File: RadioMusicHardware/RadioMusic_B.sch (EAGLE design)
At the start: 32 parts, among them IC4 TL074, U1 TEENSY_3.1_TW

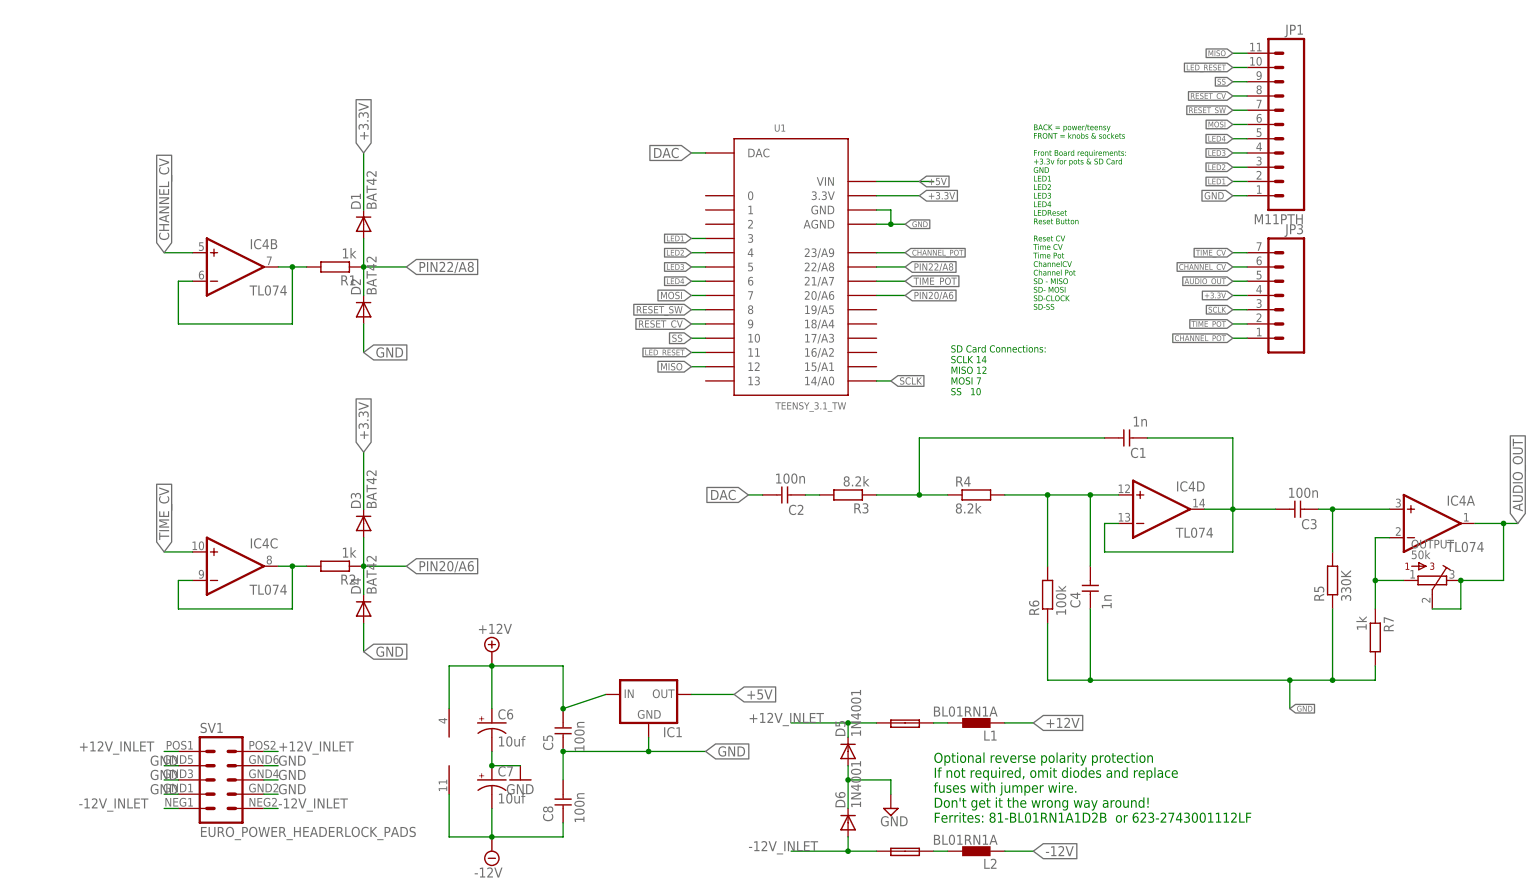
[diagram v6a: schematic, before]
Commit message: Routed Version 2 -  needs to be checked
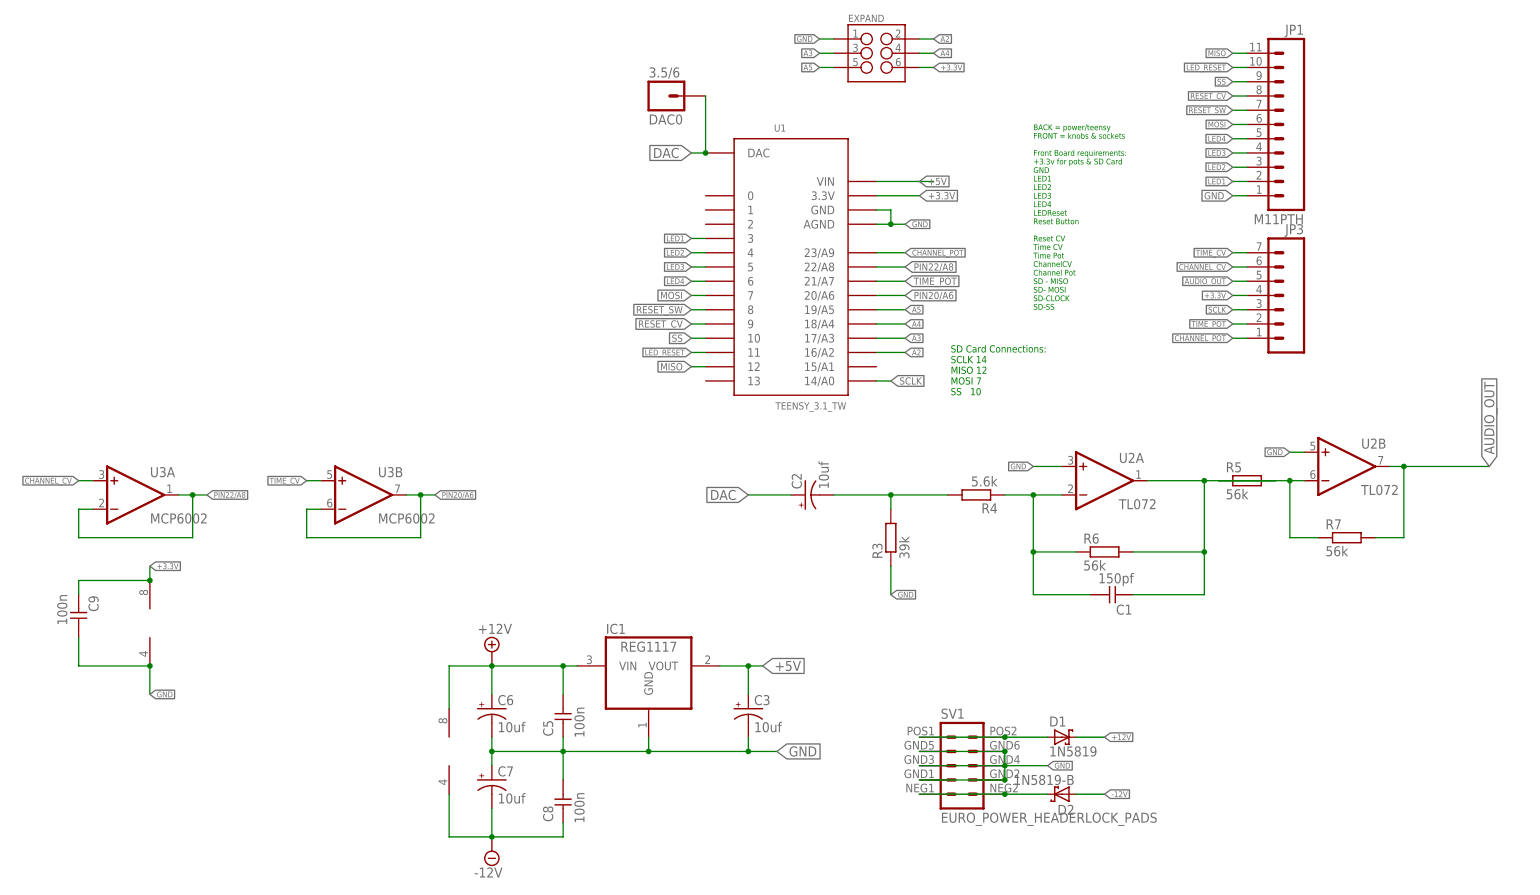
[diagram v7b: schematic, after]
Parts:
- removed C4: 1n, TomW:C-EU050-024X044
- removed D3, D4: BAT42, diode:BAT81
- removed D5, D6: 1N4001, diode:1N4004
- removed F1, F2: FUSE, TomW:PTC_FUSEPOLY_FUSE
- removed IC4: TL074, linear:TL074P
- removed L1, L2: BL01RN1A, inductors:BL01RN1A
- removed OUTPUT: 50k, bourns:3362P
- removed R1, R2: 1k, TomW:R-EU_STANDARD_RESISTOR
- added 3.5/6: DAC0, SparkFun-Connectors:M01PTH
- added C9: 100n, TomW:C-EU050-024X044
- added EXPAND: (no value), SparkFun-Connectors:M03X22X3_SILK_SM
- added U2: TL072, MusicThingModular:TL072
- added U3: MCP6002, MusicThingModular:MCP6002DIL_SMALL
- C1: value 1n -> 150pf
- C2, C3: value 100n -> 10uf; device TomW:C-EU050-025X075 -> SparkFun-Passives:CAP_POLPTH2
- D1: value BAT42 -> 1N5819; device diode:BAT81 -> diode:1N5819-B
- D2: value BAT42 -> 1N5819-B; device diode:BAT81 -> diode:1N5819-B
- IC1: value (none) -> REG1117; device v-reg:78LXX -> burr-brown:REG1117
- R3: value 8.2k -> 39k
- R4: value 8.2k -> 5.6k
- R5: value 330K -> 56k
- R6: value 100k -> 56k
- R7: value 1k -> 56k
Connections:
- removed net +12V_INLET: D5.C, F1.P$1, SV1.10, SV1.9
- removed net -12V_INLET: D6.A, F2.P$1, SV1.1, SV1.2
- removed net N$10: C2.2, R3.2
- removed net N$22: F1.P$2, L1.2
- removed net N$23: F2.P$2, L2.2
- removed net N$6: C3.2, IC4A.+IN, R5.2
- removed net N$7: IC4A.-IN, OUTPUT.1, R7.1
- new net A2: EXPAND.2, U1.16/A2
- new net A3: EXPAND.3, U1.17/A3
- new net A4: EXPAND.4, U1.18/A4
- new net A5: EXPAND.5, U1.19/A5
- new net N$9: D2.C, SV1.1, SV1.2
- net +12V: now also D1.C, IC1.VIN, U2P.V+; no longer IC1.IN, IC4P.V+, L1.1
- net +3.3V: now also C9.2, EXPAND.6, U3P.V+; no longer D1.C, D3.C
- net +5V: now also C3.+, IC1.VOUT; no longer IC1.OUT
- net -12V: now also D2.A, U2P.V-; no longer IC4P.V-, L2.1
- net AUDIO_OUT: now also R7.2, U2B.OUT; no longer IC4A.OUT, OUTPUT.2, OUTPUT.3
- net CHANNEL_CV: now also U3A.+IN; no longer IC4B.+IN
- net DAC: now also 3.5/6.1, C2.+; no longer C2.1
- net GND: now also C3.-, C9.1, EXPAND.1, R3.1, U2A.+IN, U2B.+IN, U3P.V-; no longer C4.2, D2.A, D4.A, D5.A, D6.C, R5.1, R6.1, R7.2
- net N$1: now also C2.-, R3.2, R4.2; no longer IC4C.-IN, IC4C.OUT, R2.2
- net N$2: now also C1.1, R4.1, R6.1, U2A.-IN; no longer C4.1, IC4D.+IN, R4.2, R6.2
- net N$3: now also R5.1, R7.1, U2B.-IN; no longer IC4B.-IN, IC4B.OUT, R1.2
- net N$4: now also C1.2, R5.2, R6.2, U2A.OUT; no longer C1.1, R3.1, R4.1
- net N$5: now also D1.A, SV1.10, SV1.9; no longer C1.2, C3.1, IC4D.-IN, IC4D.OUT
- net PIN20/A6: now also U3B.-IN, U3B.OUT; no longer D3.A, D4.C, R2.1
- net PIN22/A8: now also U3A.-IN, U3A.OUT; no longer D1.A, D2.C, R1.1
- net TIME_CV: now also U3B.+IN; no longer IC4C.+IN
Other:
- note removed: "Optional reverse polarity protection If not required, omit diodes and replace fuses with jumper wire. Don't get it the wrong way around! Ferrites: 81-BL01RN1A1D2B or 623-2743001112LF"
- moved on the sheet: C1, C5, C6, R3, R4, R5, R6, R7, SV1
